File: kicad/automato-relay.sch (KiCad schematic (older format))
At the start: 43 parts, among them J1 TE-3-213598-4, J2 Screw_Terminal_01x03, J3 TE-3-213598-4, J4 Screw_Terminal_01x05, J5 TE-3-213598-4, J6 TE-3-213598-4, J7 Screw_Terminal_01x05, J8 TE-3-213598-4, K1 G5LE-14, K2 G5LE-14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

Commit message: update J4/J7 footprints to Phoenix 1935190
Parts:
- J4, J7: footprint Connector_Phoenix_MC_HighVoltage:PhoenixContact_MC_1,5_5-G-5.08_1x05_P5.08mm_Horizontal -> automato-relay:PhoenixContact_1935190_1x5
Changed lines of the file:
@@
 F 0 "J4" V 6750 1100 50  0000 R CNN
 F 1 "Screw_Terminal_01x05" V 6750 1400 50  0001 R CNN
-F 2 "Connector_Phoenix_MC_HighVoltage:PhoenixContact_MC_1,5_5-G-5.08_1x05_P5.08mm_Horizontal" H 6600 1050 50  0001 C CNN
+F 2 "automato-relay:PhoenixContact_1935190_1x5" H 6600 1050 50  0001 C CNN
 F 3 "~" H 6600 1050 50  0001 C CNN
 	1    6600 1050
@@
 F 0 "J7" H 11730 2592 50  0000 L CNN
 F 1 "Screw_Terminal_01x05" H 11730 2501 50  0000 L CNN
-F 2 "Connector_Phoenix_MC_HighVoltage:PhoenixContact_MC_1,5_5-G-5.08_1x05_P5.08mm_Horizontal" H 11650 2550 50  0001 C CNN
+F 2 "automato-relay:PhoenixContact_1935190_1x5" H 11650 2550 50  0001 C CNN
 F 3 "~" H 11650 2550 50  0001 C CNN
 	1    11650 2550

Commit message: add decoupling capacitors for the 74HC595
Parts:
- added C5: 10 uF, Capacitor_SMD:C_1206_3216Metric, symbol Device:C
- added C6: 0.1 uF, Capacitor_SMD:C_1206_3216Metric, symbol Device:C
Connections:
- net 3V3: now also C5.1, C6.2
- net GND: now also C5.2, C6.1
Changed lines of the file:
@@
 U 1 1 601DDF31
 P 8750 2100
-F 0 "U1" H 8950 2750 50  0000 C CNN
+F 0 "U1" H 8550 2650 50  0000 C CNN
 F 1 "74HC595" H 9000 2650 50  0000 C CNN
 F 2 "Package_SO:SO-16_3.9x9.9mm_P1.27mm" H 8750 2100 50  0001 C CNN
@@
 Wire Wire Line
 	8300 2000 8350 2000
-Text GLabel 8750 1450 1    50   Input ~ 0
+Text GLabel 8750 1150 1    50   Input ~ 0
 3V3
 Wire Wire Line
-	8750 1450 8750 1500
+	8750 1150 8750 1250
 $Comp
 L Converter_ACDC:HLK-PM03 PS1
@@
 Wire Wire Line
 	11350 1200 11350 1250
+$Comp
+L Device:C C6
+U 1 1 60E8FC85
+P 9000 1250
+F 0 "C6" V 8748 1250 50  0000 C CNN
+F 1 "0.1 uF" V 8839 1250 50  0000 C CNN
+F 2 "Capacitor_SMD:C_1206_3216Metric" H 9038 1100 50  0001 C CNN
+F 3 "~" H 9000 1250 50  0001 C CNN
+	1    9000 1250
+	0    1    1    0
+$EndComp
+$Comp
+L Device:C C5
+U 1 1 60E90B07
+P 8500 1250
+F 0 "C5" V 8248 1250 50  0000 C CNN
+F 1 "10 uF" V 8339 1250 50  0000 C CNN
+F 2 "Capacitor_SMD:C_1206_3216Metric" H 8538 1100 50  0001 C CNN
+F 3 "~" H 8500 1250 50  0001 C CNN
+	1    8500 1250
+	0    1    1    0
+$EndComp
+Wire Wire Line
+	8650 1250 8750 1250
+$Comp
+L power:GND #PWR08
+U 1 1 60E98BD7
+P 8250 1350
+F 0 "#PWR08" H 8250 1100 50  0001 C CNN
+F 1 "GND" H 8255 1177 50  0001 C CNN
+F 2 "" H 8250 1350 50  0001 C CNN
+F 3 "" H 8250 1350 50  0001 C CNN
+	1    8250 1350
+	1    0    0    -1
+$EndComp
+$Comp
+L power:GND #PWR010
+U 1 1 60E9962C
+P 9250 1350
+F 0 "#PWR010" H 9250 1100 50  0001 C CNN
+F 1 "GND" H 9255 1177 50  0001 C CNN
+F 2 "" H 9250 1350 50  0001 C CNN
+F 3 "" H 9250 1350 50  0001 C CNN
+	1    9250 1350
+	1    0    0    -1
+$EndComp
+Wire Wire Line
+	8350 1250 8250 1250
+Wire Wire Line
+	8250 1250 8250 1350
+Wire Wire Line
+	9150 1250 9250 1250
+Wire Wire Line
+	9250 1250 9250 1350
+Connection ~ 8750 1250
+Wire Wire Line
+	8750 1250 8750 1500
+Wire Wire Line
+	8750 1250 8850 1250
 $EndSCHEMATC

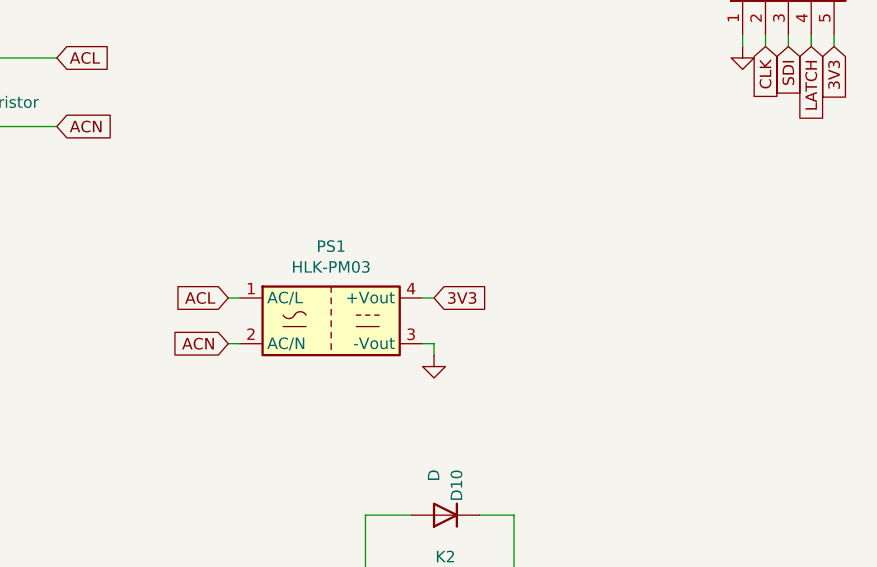
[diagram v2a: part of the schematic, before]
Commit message: add decoupling capacitor for the HLK-PM03
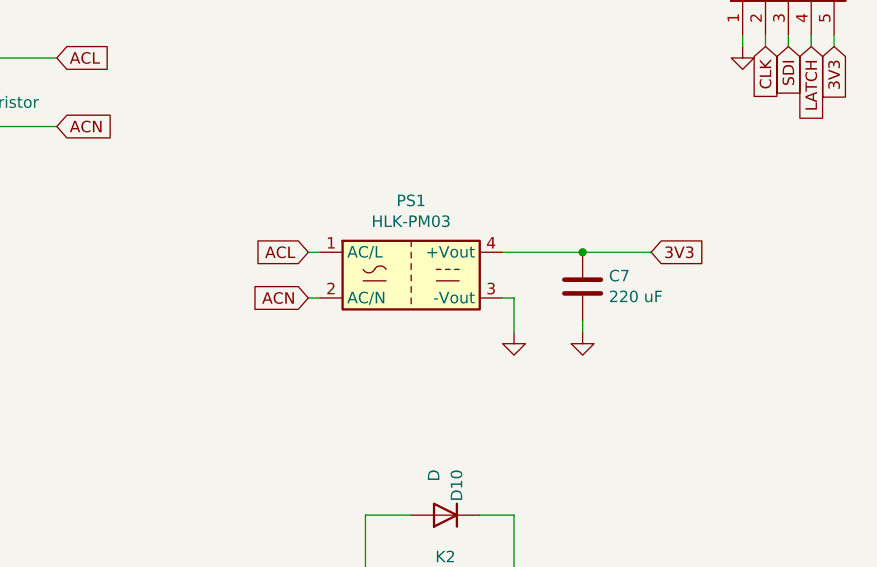
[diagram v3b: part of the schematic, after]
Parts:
- added C7: 220 uF, Capacitor_THT:CP_Radial_D6.3mm_P2.50mm, symbol Device:C
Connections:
- net 3V3: now also C7.1
- net GND: now also C7.2
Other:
- moved on the sheet: PS1
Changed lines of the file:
@@
 L Converter_ACDC:HLK-PM03 PS1
 U 1 1 602425FA
-P 4600 2500
-F 0 "PS1" H 4600 2825 50  0000 C CNN
-F 1 "HLK-PM03" H 4600 2734 50  0000 C CNN
-F 2 "Converter_ACDC:Converter_ACDC_HiLink_HLK-PMxx" H 4600 2200 50  0001 C CNN
-F 3 "http://www.hlktech.net/product_detail.php?ProId=59" H 5000 2150 50  0001 C CNN
-	1    4600 2500
-	1    0    0    -1
-$EndComp
-$Comp
-L power:GND #PWR05
-U 1 1 60242AA4
-P 5050 2650
-F 0 "#PWR05" H 5050 2400 50  0001 C CNN
-F 1 "GND" H 5055 2477 50  0001 C CNN
-F 2 "" H 5050 2650 50  0001 C CNN
-F 3 "" H 5050 2650 50  0001 C CNN
-	1    5050 2650
-	1    0    0    -1
-$EndComp
-Wire Wire Line
-	5000 2600 5050 2600
-Wire Wire Line
-	5050 2600 5050 2650
-Text GLabel 5050 2400 2    50   Input ~ 0
+P 4950 2300
+F 0 "PS1" H 4950 2625 50  0000 C CNN
+F 1 "HLK-PM03" H 4950 2534 50  0000 C CNN
+F 2 "Converter_ACDC:Converter_ACDC_HiLink_HLK-PMxx" H 4950 2000 50  0001 C CNN
+F 3 "http://www.hlktech.net/product_detail.php?ProId=59" H 5350 1950 50  0001 C CNN
+	1    4950 2300
+	1    0    0    -1
+$EndComp
+Text GLabel 6000 2200 2    50   Input ~ 0
 3V3
 Wire Wire Line
-	5000 2400 5050 2400
-Text GLabel 4150 2600 0    50   Input ~ 0
+	5350 2200 5700 2200
+Text GLabel 4500 2400 0    50   Input ~ 0
 ACN
 Text GLabel 1150 5250 0    50   Input ~ 0
 ACN
 Wire Wire Line
-	4150 2600 4200 2600
-Wire Wire Line
-	4150 2400 4200 2400
-Text GLabel 4150 2400 0    50   Input ~ 0
+	4500 2400 4550 2400
+Wire Wire Line
+	4500 2200 4550 2200
+Text GLabel 4500 2200 0    50   Input ~ 0
 ACL
 Text GLabel 3400 1350 2    50   Input ~ 0
@@
 Wire Wire Line
 	8750 1250 8850 1250
+$Comp
+L power:GND #PWR05
+U 1 1 60242AA4
+P 5400 2550
+F 0 "#PWR05" H 5400 2300 50  0001 C CNN
+F 1 "GND" H 5405 2377 50  0001 C CNN
+F 2 "" H 5400 2550 50  0001 C CNN
+F 3 "" H 5400 2550 50  0001 C CNN
+	1    5400 2550
+	1    0    0    -1
+$EndComp
+Wire Wire Line
+	5400 2400 5400 2550
+Wire Wire Line
+	5350 2400 5400 2400
+$Comp
+L Device:C C7
+U 1 1 60EB3F05
+P 5700 2350
+F 0 "C7" H 5815 2396 50  0000 L CNN
+F 1 "220 uF" H 5815 2305 50  0000 L CNN
+F 2 "Capacitor_THT:CP_Radial_D6.3mm_P2.50mm" H 5738 2200 50  0001 C CNN
+F 3 "~" H 5700 2350 50  0001 C CNN
+	1    5700 2350
+	1    0    0    -1
+$EndComp
+Connection ~ 5700 2200
+Wire Wire Line
+	5700 2200 6000 2200
+$Comp
+L power:GND #PWR011
+U 1 1 60EC1592
+P 5700 2550
+F 0 "#PWR011" H 5700 2300 50  0001 C CNN
+F 1 "GND" H 5705 2377 50  0001 C CNN
+F 2 "" H 5700 2550 50  0001 C CNN
+F 3 "" H 5700 2550 50  0001 C CNN
+	1    5700 2550
+	1    0    0    -1
+$EndComp
+Wire Wire Line
+	5700 2500 5700 2550
 $EndSCHEMATC

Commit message: add X1 safety capacitor across AC lines
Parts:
- added C8: 1 nF, Capacitor_THT:C_Disc_D7.5mm_W5.0mm_P10.00mm, symbol Device:C
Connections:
- net ACL: now also C8.1
- net ACN: now also C8.2
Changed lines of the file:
@@
 Text GLabel 4500 2200 0    50   Input ~ 0
 ACL
-Text GLabel 3400 1350 2    50   Input ~ 0
+Text GLabel 3800 1350 2    50   Input ~ 0
 ACL
-Text GLabel 3400 1650 2    50   Input ~ 0
+Text GLabel 3800 1650 2    50   Input ~ 0
 ACN
 Text GLabel 12550 5250 2    50   Input ~ 0
@@
 Connection ~ 2950 1350
 Wire Wire Line
-	2950 1350 3400 1350
+	2950 1350 3500 1350
 Wire Wire Line
 	2650 1550 2650 1650
@@
 Connection ~ 2950 1650
 Wire Wire Line
-	2950 1650 3400 1650
+	2950 1650 3500 1650
 Wire Wire Line
 	2400 1650 2400 1850
@@
 Wire Wire Line
 	5700 2500 5700 2550
+$Comp
+L Device:C C8
+U 1 1 60E8BDAC
+P 3500 1500
+F 0 "C8" H 3615 1546 50  0000 L CNN
+F 1 "1 nF" H 3615 1455 50  0000 L CNN
+F 2 "Capacitor_THT:C_Disc_D7.5mm_W5.0mm_P10.00mm" H 3538 1350 50  0001 C CNN
+F 3 "~" H 3500 1500 50  0001 C CNN
+	1    3500 1500
+	1    0    0    -1
+$EndComp
+Connection ~ 3500 1350
+Wire Wire Line
+	3500 1350 3800 1350
+Connection ~ 3500 1650
+Wire Wire Line
+	3500 1650 3800 1650
 $EndSCHEMATC

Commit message: Changed Indicator bypass diodes to 1000V reverse-voltage diodes (1n4007)
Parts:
- D1, D3, D5, D7: footprint Diode_SMD:D_SOT-23_ANK -> Diode_SMD:D_SOD-123

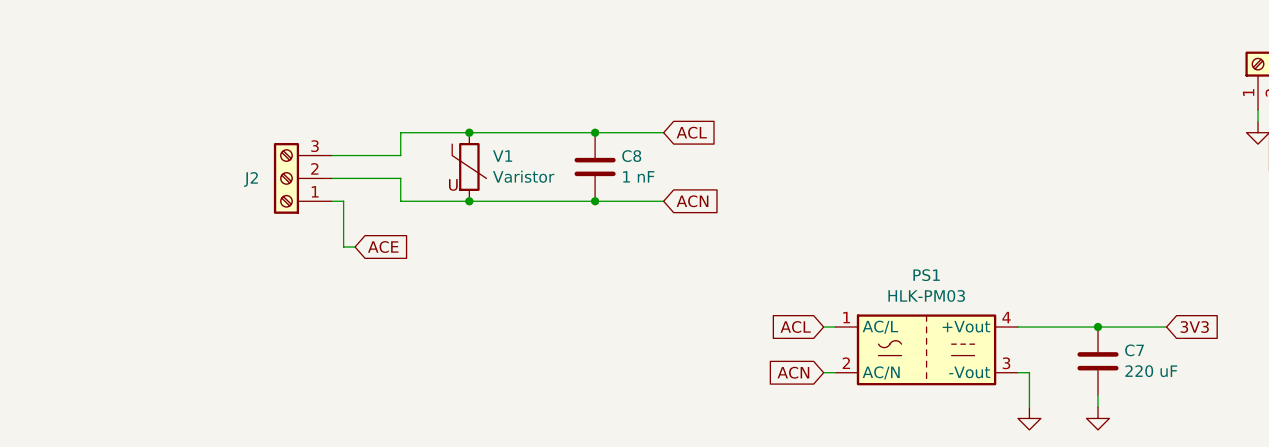
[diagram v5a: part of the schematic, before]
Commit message: removed screw terminals, add IEC inlet + switch
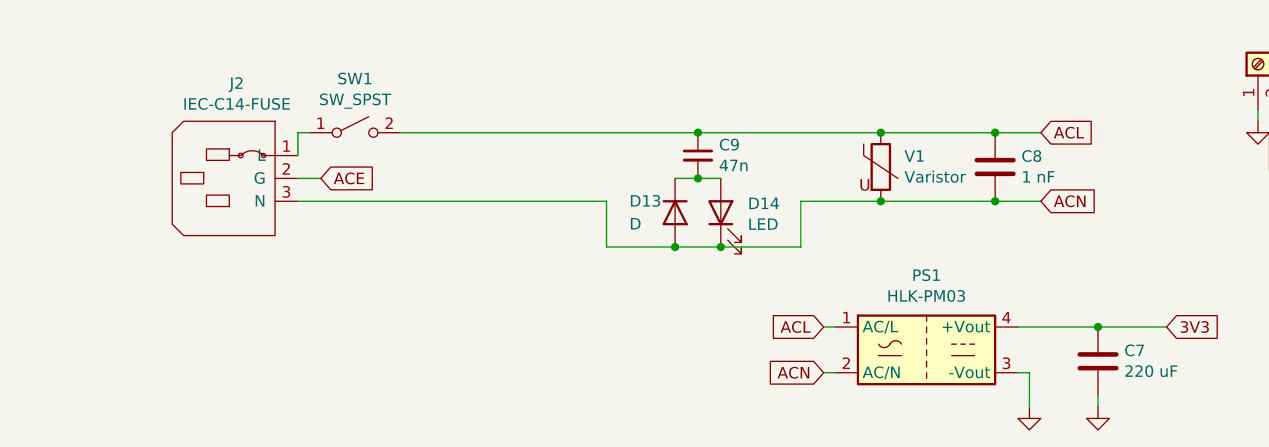
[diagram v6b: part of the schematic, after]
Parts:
- removed J2: Screw_Terminal_01x03, Connector_Phoenix_MC_HighVoltage:PhoenixContact_MCV_1,5_3-G-5.08_1x03_P5.08mm_Vertical, symbol Connector:Screw_Terminal_01x03
- added C9: 47n, Capacitor_SMD:C_1206_3216Metric, symbol Device:C_Small
- added D13: D, Diode_SMD:D_SOD-123, symbol Device:D
- added D14: LED, LED_SMD:LED_1206_3216Metric, symbol Device:LED
- added J2: IEC-C14-FUSE, automato-relay:PF0011-15-PC, symbol automato-relay:IEC-C14-FUSE
- added SW1: SW_SPST, automato-relay:RA1H1C112R, symbol Switch:SW_SPST
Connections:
- net ACE: now also J2.2 (G)
- net ACL: now also C9.1, SW1.2 (B)
- net ACN: now also D13.2 (A), D14.1 (K), J2.3 (N)
- new net: J2.1 (L), SW1.1 (A)
- new net: C9.2, D13.1 (K), D14.2 (A)
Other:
- moved on the sheet: C8, V1
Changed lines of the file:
@@
 Text GLabel 4500 2200 0    50   Input ~ 0
 ACL
-Text GLabel 3800 1350 2    50   Input ~ 0
+Text GLabel 5450 1350 2    50   Input ~ 0
 ACL
-Text GLabel 3800 1650 2    50   Input ~ 0
+Text GLabel 5450 1650 2    50   Input ~ 0
 ACN
 Text GLabel 12550 5250 2    50   Input ~ 0
@@
 Text GLabel 2850 3900 2    50   Input ~ 0
 3V3
-$Comp
-L Connector:Screw_Terminal_01x03 J2
-U 1 1 602EE614
-P 2150 1550
-F 0 "J2" H 2300 1550 50  0000 C CNN
-F 1 "Screw_Terminal_01x03" H 2068 1316 50  0001 C CNN
-F 2 "Connector_Phoenix_MC_HighVoltage:PhoenixContact_MCV_1,5_3-G-5.08_1x03_P5.08mm_Vertical" H 2150 1550 50  0001 C CNN
-F 3 "~" H 2150 1550 50  0001 C CNN
-	1    2150 1550
-	-1   0    0    1
-$EndComp
-Text GLabel 2450 1850 2    50   Input ~ 0
+Text GLabel 2300 1550 2    50   Input ~ 0
 ACE
-Wire Wire Line
-	2350 1650 2400 1650
 Text GLabel 12050 5850 3    50   Input ~ 0
 ACE
@@
 L Device:Varistor V1
 U 1 1 60401D0D
-P 2950 1500
-F 0 "V1" H 3053 1546 50  0000 L CNN
-F 1 "Varistor" H 3053 1455 50  0000 L CNN
-F 2 "Varistor:RV_Disc_D15.5mm_W3.9mm_P7.5mm" V 2880 1500 50  0001 C CNN
-F 3 "~" H 2950 1500 50  0001 C CNN
-	1    2950 1500
-	1    0    0    -1
-$EndComp
-Wire Wire Line
-	2650 1450 2650 1350
-Wire Wire Line
-	2650 1350 2950 1350
-Wire Wire Line
-	2350 1450 2650 1450
-Connection ~ 2950 1350
-Wire Wire Line
-	2950 1350 3500 1350
-Wire Wire Line
-	2650 1550 2650 1650
-Wire Wire Line
-	2650 1650 2950 1650
-Wire Wire Line
-	2350 1550 2650 1550
-Connection ~ 2950 1650
-Wire Wire Line
-	2950 1650 3500 1650
-Wire Wire Line
-	2400 1650 2400 1850
-Wire Wire Line
-	2400 1850 2450 1850
+P 4750 1500
+F 0 "V1" H 4853 1546 50  0000 L CNN
+F 1 "Varistor" H 4853 1455 50  0000 L CNN
+F 2 "Varistor:RV_Disc_D15.5mm_W3.9mm_P7.5mm" V 4680 1500 50  0001 C CNN
+F 3 "~" H 4750 1500 50  0001 C CNN
+	1    4750 1500
+	1    0    0    -1
+$EndComp
+Wire Wire Line
+	4750 1350 5250 1350
+Wire Wire Line
+	4750 1650 5250 1650
 $Comp
 L Connector:TestPoint TP1
@@
 L Device:C C8
 U 1 1 60E8BDAC
-P 3500 1500
-F 0 "C8" H 3615 1546 50  0000 L CNN
-F 1 "1 nF" H 3615 1455 50  0000 L CNN
-F 2 "Capacitor_THT:C_Disc_D7.5mm_W5.0mm_P10.00mm" H 3538 1350 50  0001 C CNN
-F 3 "~" H 3500 1500 50  0001 C CNN
-	1    3500 1500
-	1    0    0    -1
-$EndComp
-Connection ~ 3500 1350
-Wire Wire Line
-	3500 1350 3800 1350
-Connection ~ 3500 1650
-Wire Wire Line
-	3500 1650 3800 1650
+P 5250 1500
+F 0 "C8" H 5365 1546 50  0000 L CNN
+F 1 "1 nF" H 5365 1455 50  0000 L CNN
+F 2 "Capacitor_THT:C_Disc_D7.5mm_W5.0mm_P10.00mm" H 5288 1350 50  0001 C CNN
+F 3 "~" H 5250 1500 50  0001 C CNN
+	1    5250 1500
+	1    0    0    -1
+$EndComp
+Wire Wire Line
+	5250 1350 5450 1350
+Wire Wire Line
+	5250 1650 5450 1650
 $Comp
 L Device:D D11
@@
 	-1   0    0    1
 $EndComp
+Wire Wire Line
+	2200 1550 2300 1550
+Wire Wire Line
+	2250 1350 2200 1350
+Wire Wire Line
+	2200 1350 2200 1450
+Connection ~ 5250 1350
+Connection ~ 5250 1650
+$Comp
+L Device:LED D14
+U 1 1 6218C0A6
+P 4050 1700
+F 0 "D14" V 4089 1582 50  0000 R CNN
+F 1 "LED" V 3998 1582 50  0000 R CNN
+F 2 "LED_SMD:LED_1206_3216Metric" H 4050 1700 50  0001 C CNN
+F 3 "~" H 4050 1700 50  0001 C CNN
+	1    4050 1700
+	0    -1   -1   0
+$EndComp
+$Comp
+L Device:D D13
+U 1 1 6218C0AC
+P 3850 1700
+F 0 "D13" V 3800 1500 50  0000 L CNN
+F 1 "D" V 3900 1500 50  0000 L CNN
+F 2 "Diode_SMD:D_SOD-123" H 3850 1700 50  0001 C CNN
+F 3 "~" H 3850 1700 50  0001 C CNN
+	1    3850 1700
+	0    1    1    0
+$EndComp
+Wire Wire Line
+	3850 1550 3950 1550
+Connection ~ 3950 1550
+Wire Wire Line
+	3950 1550 4050 1550
+$Comp
+L Device:C_Small C9
+U 1 1 6218C0BB
+P 3950 1450
+F 0 "C9" H 4042 1496 50  0000 L CNN
+F 1 "47n" H 4042 1405 50  0000 L CNN
+F 2 "Capacitor_SMD:C_1206_3216Metric" H 3950 1450 50  0001 C CNN
+F 3 "~" H 3950 1450 50  0001 C CNN
+	1    3950 1450
+	1    0    0    -1
+$EndComp
+Connection ~ 4750 1350
+Connection ~ 3950 1350
+Wire Wire Line
+	3950 1350 4750 1350
+Wire Wire Line
+	2200 1650 3550 1650
+Wire Wire Line
+	3550 1650 3550 1850
+Wire Wire Line
+	4400 1850 4400 1650
+Wire Wire Line
+	4400 1650 4750 1650
+Wire Wire Line
+	3550 1850 3850 1850
+Connection ~ 3850 1850
+Wire Wire Line
+	3850 1850 4050 1850
+Connection ~ 4050 1850
+Wire Wire Line
+	4050 1850 4400 1850
+Connection ~ 4750 1650
+Wire Wire Line
+	2650 1350 3950 1350
+$Comp
+L automato-relay:IEC-C14-FUSE J2
+U 1 1 62295365
+P 1950 1550
+F 0 "J2" H 1933 1965 50  0000 C CNN
+F 1 "IEC-C14-FUSE" H 1933 1874 50  0000 C CNN
+F 2 "automato-relay:PF0011-15-PC" V 1950 1550 50  0001 C CNN
+F 3 "" V 1950 1550 50  0001 C CNN
+	1    1950 1550
+	1    0    0    -1
+$EndComp
+$Comp
+L Switch:SW_SPST SW1
+U 1 1 62108163
+P 2450 1350
+F 0 "SW1" H 2450 1585 50  0000 C CNN
+F 1 "SW_SPST" H 2450 1494 50  0000 C CNN
+F 2 "automato-relay:RA1H1C112R" H 2450 1350 50  0001 C CNN
+F 3 "~" H 2450 1350 50  0001 C CNN
+	1    2450 1350
+	1    0    0    -1
+$EndComp
 $EndSCHEMATC
